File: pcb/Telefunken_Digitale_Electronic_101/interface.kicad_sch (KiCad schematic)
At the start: 3 parts

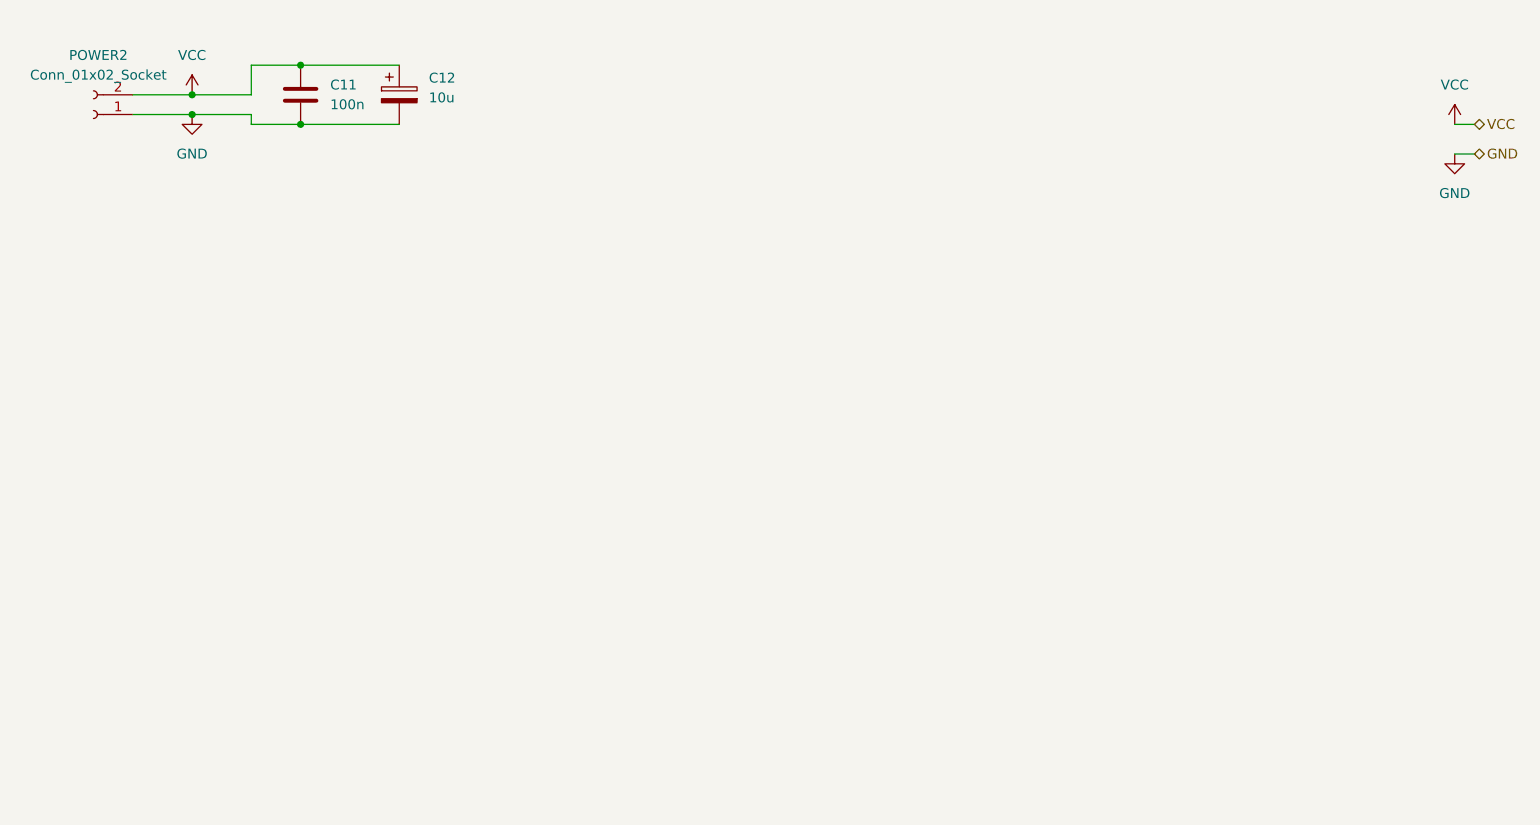
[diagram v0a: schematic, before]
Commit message: SCH - interface: added connectors (JST connectors) and labels
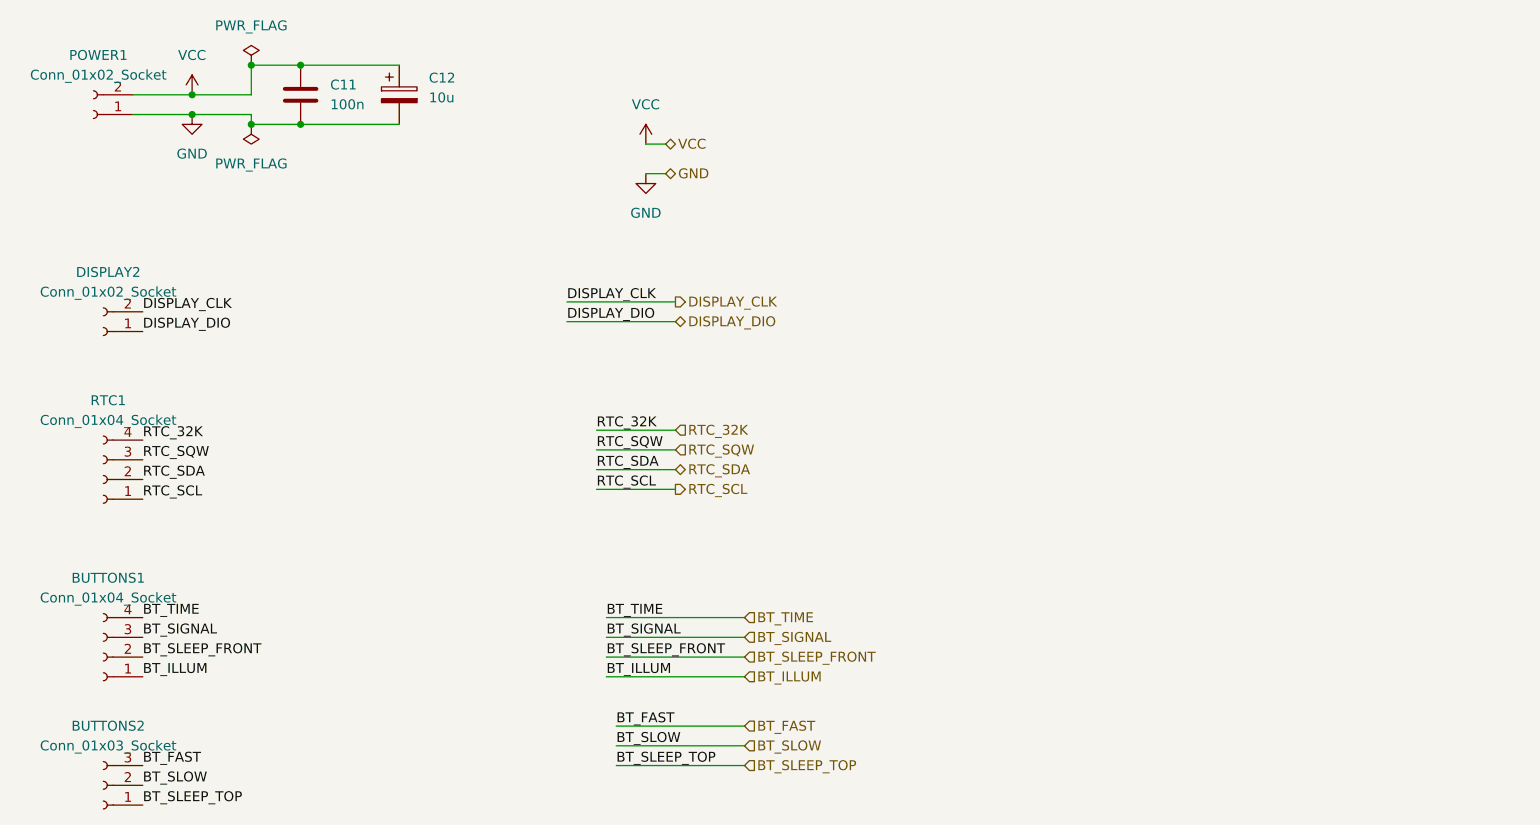
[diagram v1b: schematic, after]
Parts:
- added BUTTONS1, RTC1: Conn_01x04_Socket, Connector_JST:JST_GH_BM04B-GHS-TBT_1x04-1MP_P1.25mm_Vertical, symbol Connector:Conn_01x04_Socket
- added BUTTONS2: Conn_01x03_Socket, Connector_JST:JST_GH_BM03B-GHS-TBT_1x03-1MP_P1.25mm_Vertical, symbol Connector:Conn_01x03_Socket
- added DISPLAY2: Conn_01x02_Socket, Connector_JST:JST_GH_BM02B-GHS-TBT_1x02-1MP_P1.25mm_Vertical, symbol Connector:Conn_01x02_Socket
- POWER1: renamed from POWER2; footprint (none) -> Connector_JST:JST_XH_B2B-XH-A_1x02_P2.50mm_Vertical
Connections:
- new net BT_FAST: BUTTONS2.3 (Pin_3)
- new net BT_ILLUM: BUTTONS1.1 (Pin_1)
- new net BT_SIGNAL: BUTTONS1.3 (Pin_3)
- new net BT_SLEEP_FRONT: BUTTONS1.2 (Pin_2)
- new net BT_SLEEP_TOP: BUTTONS2.1 (Pin_1)
- new net BT_SLOW: BUTTONS2.2 (Pin_2)
- new net BT_TIME: BUTTONS1.4 (Pin_4)
- new net DISPLAY_CLK: DISPLAY2.2 (Pin_2)
- new net DISPLAY_DIO: DISPLAY2.1 (Pin_1)
- new net RTC_32K: RTC1.4 (Pin_4)
- new net RTC_SCL: RTC1.1 (Pin_1)
- new net RTC_SDA: RTC1.2 (Pin_2)
- new net RTC_SQW: RTC1.3 (Pin_3)
